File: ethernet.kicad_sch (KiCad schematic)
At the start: 94 parts, among them IC2 ACPL-217-500E, J2 5-2337992-8, U13 TPS2372-3RGWR, U16 TS3L500, U6 KSZ9031RNXCA, Y1 ABM8G-25.000MHZ-18-D2Y-T

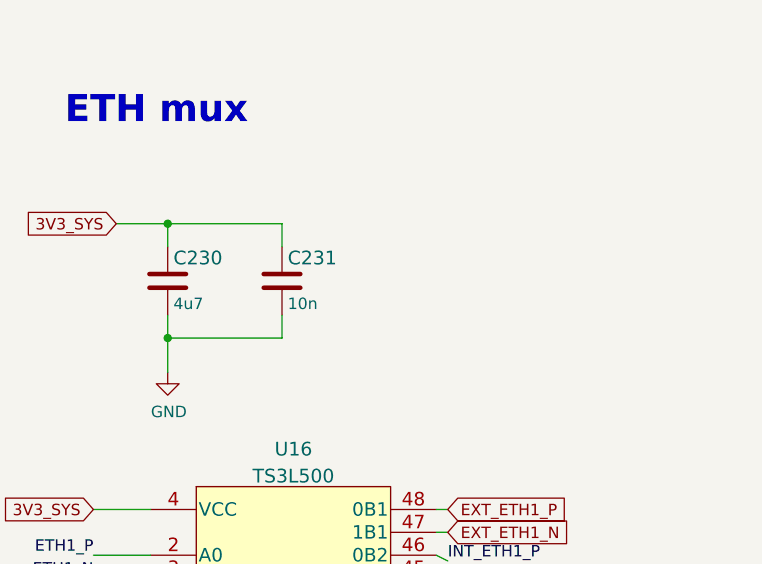
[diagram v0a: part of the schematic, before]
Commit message: Route internal end external (FMC) ETH interface, add additional VDDQ and ETH MUX decoupling
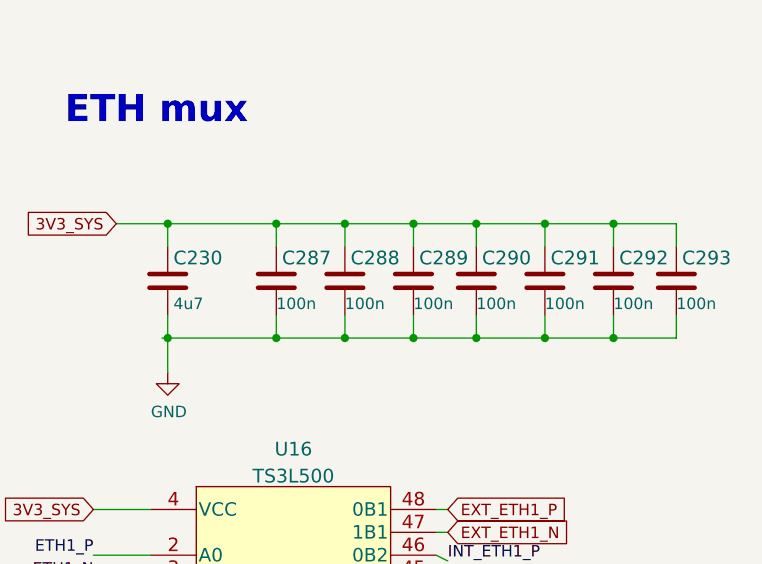
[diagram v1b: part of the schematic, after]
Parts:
- removed C231: C_10n_0402, data-center-dram-tester-footprints:0402-cap, symbol data-center-dram-tester:C_10n_0402
- added C287, C288, C289, C290, C291, C292, C293: C_100n_0402, antmicro-footprints:0402-cap, symbol antmicroCapacitors0402:C_100n_0402
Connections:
- net GND: now also C287.2, C288.2, C289.2, C290.2, C291.2, C292.2, C293.2
- net VCC: now also C287.1, C288.1, C289.1, C290.1, C291.1, C292.1, C293.1

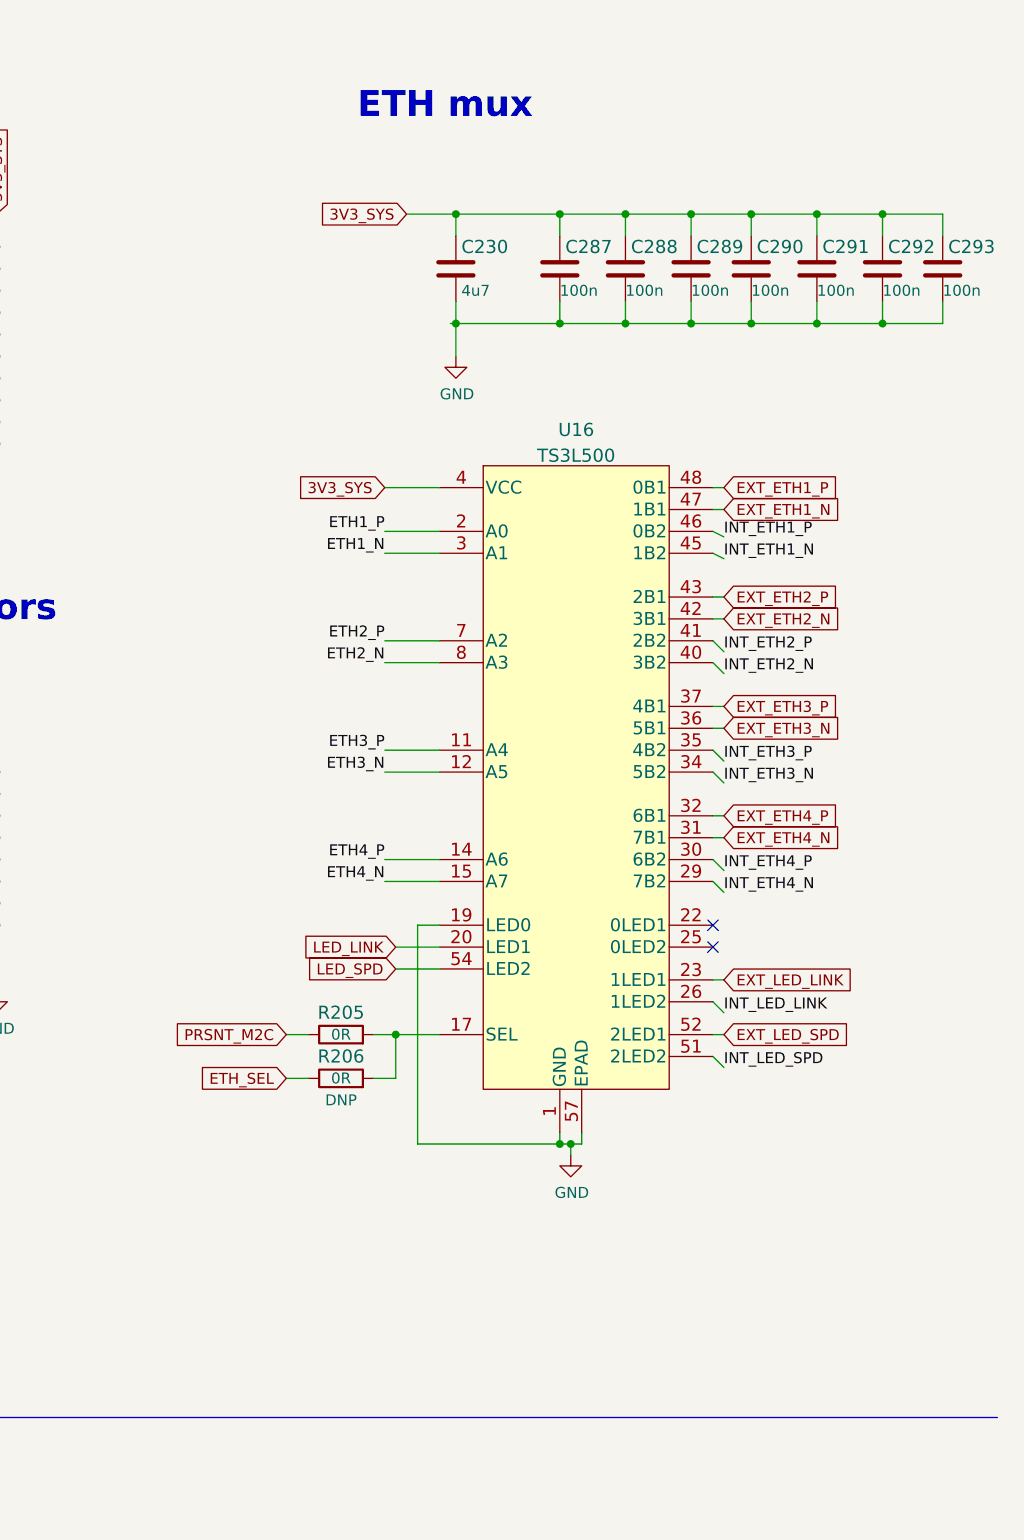
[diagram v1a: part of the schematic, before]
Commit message: Add ETH MUX passthrough, reroute HDMI to 100 Ohm differential, begin routing current measurment circuit
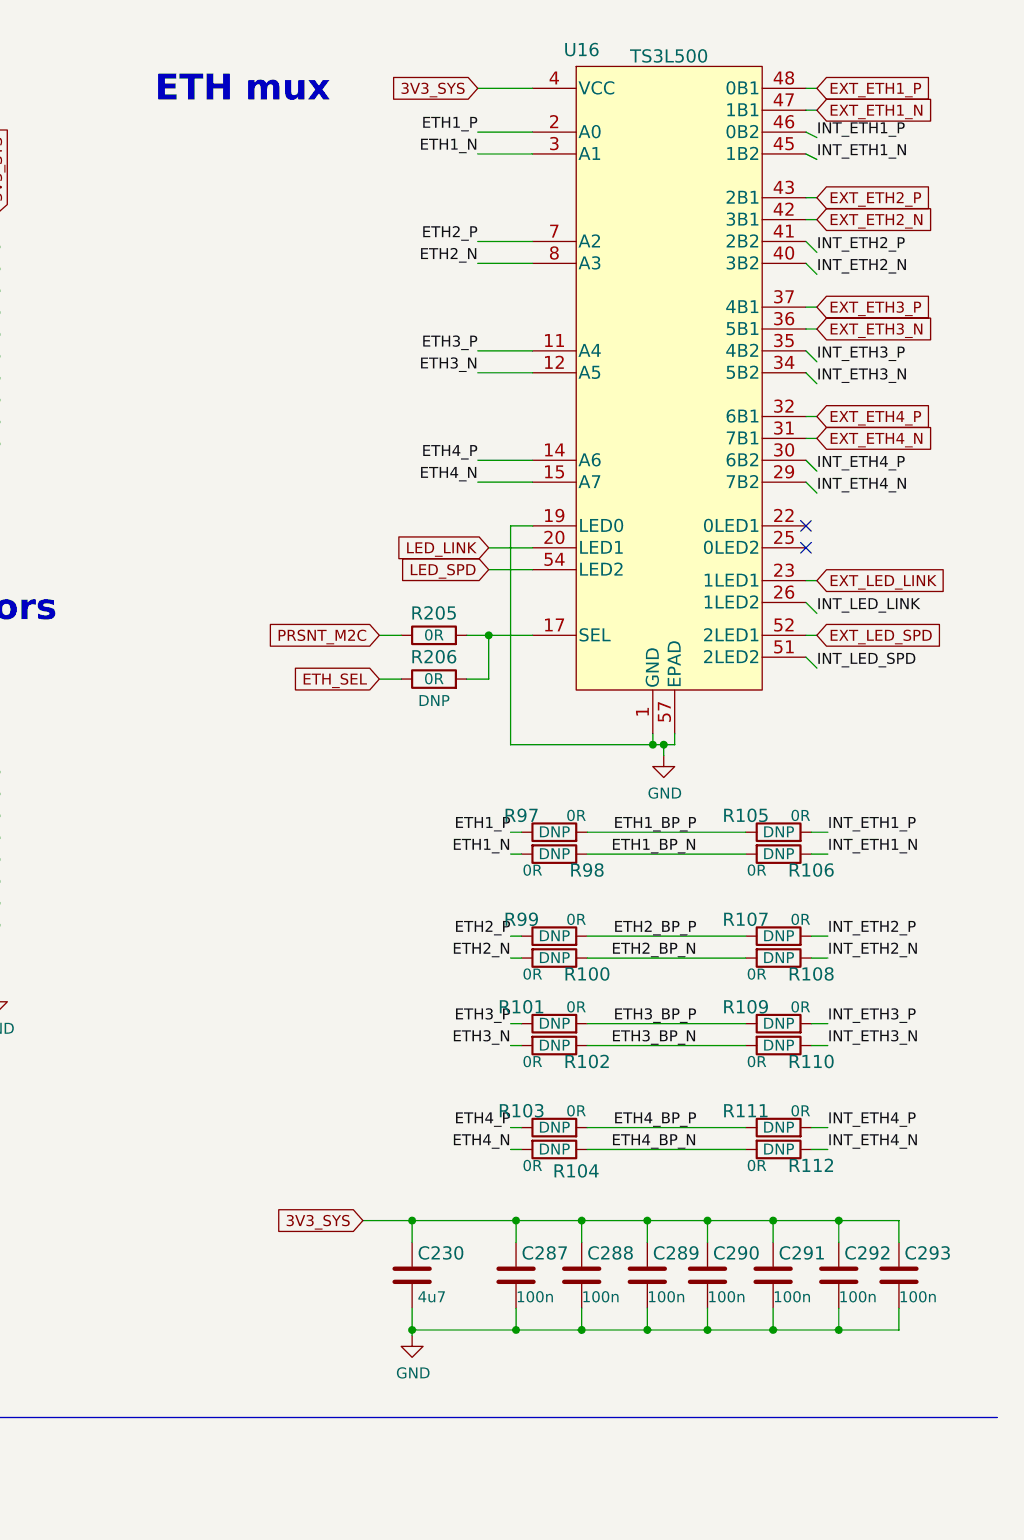
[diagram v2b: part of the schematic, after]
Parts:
- added R100, R101, R102, R103, R104, R105, R106, R107, R108, R109, R110, R111, R112, R97, R98, R99: R_0R_0201, antmicro-footprints:0201-res, symbol antmicroResistorsmisc:R_0R_0201
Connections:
- net ETH1_N: now also R98.2
- net ETH1_P: now also R97.1
- net ETH2_N: now also R100.2
- net ETH2_P: now also R99.1
- net ETH3_N: now also R102.2
- net ETH3_P: now also R101.1
- net ETH4_N: now also R104.2
- net ETH4_P: now also R103.1
- net INT_ETH1_N: now also R106.1
- net INT_ETH1_P: now also R105.2
- net INT_ETH2_N: now also R108.1
- net INT_ETH2_P: now also R107.2
- net INT_ETH3_N: now also R110.1
- net INT_ETH3_P: now also R109.2
- net INT_ETH4_N: now also R112.1
- net INT_ETH4_P: now also R111.2
- new net ETH1_BP_N: R106.2, R98.1
- new net ETH1_BP_P: R105.1, R97.2
- new net ETH2_BP_N: R100.1, R108.2
- new net ETH2_BP_P: R107.1, R99.2
- new net ETH3_BP_N: R102.1, R110.2
- new net ETH3_BP_P: R101.2, R109.1
- new net ETH4_BP_N: R104.1, R112.2
- new net ETH4_BP_P: R103.2, R111.1
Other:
- moved on the sheet: C230, C287, C288, C289, C290, C291, C292, C293, R205, R206, U16

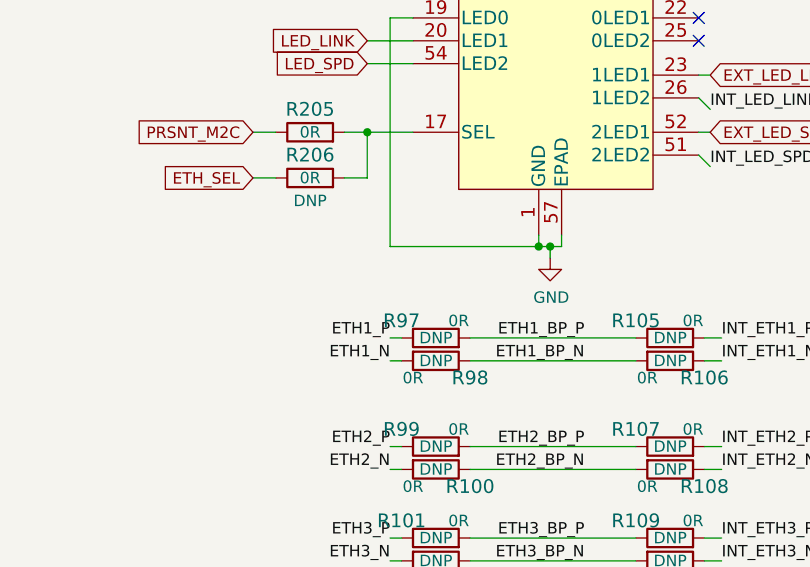
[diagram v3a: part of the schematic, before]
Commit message: Add missing FMC vias, route: MODE, JTAG, active discharge, reconnect 5V buses
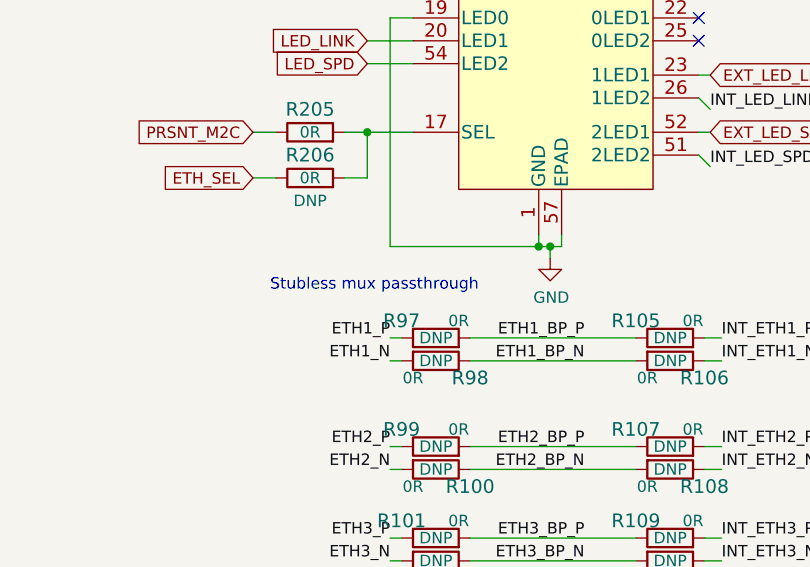
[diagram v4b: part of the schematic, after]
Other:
- note added: "Stubless mux passthrough"
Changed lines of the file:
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@@
     (effects (font (size 2.9972 2.9972) (thickness 0.5994) bold) (justify left bottom))
+  )
+  (text "Stubless mux passthrough" (at 339.09 102.235 0)
+    (effects (font (size 1.27 1.27)) (justify left bottom))
   )
   (label "INT_ETH4_N" (at 387.985 67.945 0)

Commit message: Finish power supply polygons, improve connector shield to ground connection
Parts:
- removed FB7: BLM18PG121SN1D, data-center-dram-tester-footprints:0603-res, symbol data-center-dram-tester:BLM18PG121SN1D
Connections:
- net GNDS: now reaches J2.19 (SHIELD1), J2.20 (SHIELD2)
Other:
- moved on the sheet: IC2, R183, R184

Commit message: Finish routing all connections
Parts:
- removed C221: C_10n_0402, data-center-dram-tester-footprints:0402-cap, symbol data-center-dram-tester:C_10n_0402
- added C221, C312: C_100n_0402, data-center-dram-tester-footprints:0402-cap, symbol data-center-dram-tester:C_100n_0402_16V
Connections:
- net GND: now also C221.2, C312.2
- net at J2.5 (P5): now also C312.1; no longer J2.4 (P4)
- new net: C221.1, J2.4 (P4)
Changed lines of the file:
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@@
   (junction (at 292.735 102.87) (diameter 0) (color 0 0 0 0)
   )
-  (junction (at 43.18 240.665) (diameter 0) (color 0 0 0 0)
-  )
   (junction (at 292.735 107.95) (diameter 0) (color 0 0 0 0)
   )
@@
   (junction (at 266.065 199.39) (diameter 0) (color 0 0 0 0)
   )
+  (junction (at 23.495 259.715) (diameter 0) (color 0 0 0 0)
+  )
   (junction (at 41.275 31.75) (diameter 0) (color 0 0 0 0)
   )
@@
     (stroke (width 0) (type default) (color 0 0 0 0))
   )
-  (wire (pts (xy 36.195 259.715) (xy 36.195 261.62))
+  (wire (pts (xy 23.495 255.905) (xy 23.495 259.715))
     (stroke (width 0) (type default) (color 0 0 0 0))
   )
@@
     (stroke (width 0) (type default) (color 0 0 0 0))
   )
-  (wire (pts (xy 44.45 243.205) (xy 43.18 243.205))
-    (stroke (width 0) (type default) (color 0 0 0 0))
-  )
   (wire (pts (xy 205.105 141.605) (xy 205.105 147.955))
     (stroke (width 0) (type default) (color 0 0 0 0))
@@
     (stroke (width 0) (type default) (color 0 0 0 0))
   )
+  (wire (pts (xy 31.75 243.205) (xy 31.75 248.285))
+    (stroke (width 0) (type default) (color 0 0 0 0))
+  )
   (wire (pts (xy 353.06 162.56) (xy 353.06 165.1))
     (stroke (width 0) (type default) (color 0 0 0 0))
@@
     (stroke (width 0) (type default) (color 0 0 0 0))
   )
-  (wire (pts (xy 43.18 240.665) (xy 43.18 243.205))
-    (stroke (width 0) (type default) (color 0 0 0 0))
-  )
   (wire (pts (xy 210.185 60.325) (xy 210.185 54.61))
     (stroke (width 0) (type default) (color 0 0 0 0))
@@
     (stroke (width 0) (type default) (color 0 0 0 0))
   )
+  (wire (pts (xy 23.495 259.715) (xy 31.75 259.715))
+    (stroke (width 0) (type default) (color 0 0 0 0))
+  )
   (wire (pts (xy 352.425 132.08) (xy 353.695 132.08))
     (stroke (width 0) (type default) (color 0 0 0 0))
@@
     (stroke (width 0) (type default) (color 0 0 0 0))
   )
+  (wire (pts (xy 31.75 243.205) (xy 44.45 243.205))
+    (stroke (width 0) (type default) (color 0 0 0 0))
+  )
   (wire (pts (xy 161.925 95.885) (xy 160.655 95.885))
     (stroke (width 0) (type default) (color 0 0 0 0))
@@
     (stroke (width 0) (type default) (color 0 0 0 0))
   )
-  (wire (pts (xy 44.45 240.665) (xy 43.18 240.665))
-    (stroke (width 0) (type default) (color 0 0 0 0))
-  )
   (wire (pts (xy 372.11 243.84) (xy 373.38 243.84))
     (stroke (width 0) (type default) (color 0 0 0 0))
@@
     (stroke (width 0) (type default) (color 0 0 0 0))
   )
+  (wire (pts (xy 31.75 259.715) (xy 31.75 255.905))
+    (stroke (width 0) (type default) (color 0 0 0 0))
+  )
   (wire (pts (xy 370.205 98.425) (xy 370.205 97.155))
     (stroke (width 0) (type default) (color 0 0 0 0))
@@
     (stroke (width 0) (type default) (color 0 0 0 0))
   )
+  (wire (pts (xy 23.495 259.715) (xy 23.495 261.62))
+    (stroke (width 0) (type default) (color 0 0 0 0))
+  )
   (wire (pts (xy 283.845 64.77) (xy 292.735 64.77))
     (stroke (width 0) (type default) (color 0 0 0 0))
@@
     (stroke (width 0) (type default) (color 0 0 0 0))
   )
+  (wire (pts (xy 23.495 240.665) (xy 44.45 240.665))
+    (stroke (width 0) (type default) (color 0 0 0 0))
+  )
   (wire (pts (xy 219.075 234.95) (xy 212.725 234.95))
     (stroke (width 0) (type default) (color 0 0 0 0))
@@
     (stroke (width 0) (type default) (color 0 0 0 0))
   )
-  (wire (pts (xy 36.195 240.665) (xy 36.195 252.095))
+  (wire (pts (xy 23.495 240.665) (xy 23.495 248.285))
     (stroke (width 0) (type default) (color 0 0 0 0))
   )
@@
     (stroke (width 0) (type default) (color 0 0 0 0))
   )
-  (wire (pts (xy 43.18 240.665) (xy 36.195 240.665))
-    (stroke (width 0) (type default) (color 0 0 0 0))
-  )
   (wire (pts (xy 387.985 48.895) (xy 386.715 48.895))
     (stroke (width 0) (type default) (color 0 0 0 0))
@@
     (pin "1")
   )
-  (symbol (lib_id "data-center-dram-tester:GND") (at 36.195 261.62 0) (unit 1)
+  (symbol (lib_id "data-center-dram-tester:GND") (at 23.495 261.62 0) (unit 1)
     (in_bom yes) (on_board yes)
-    (property "Reference" "#PWR042" (id 0) (at 36.195 267.97 0)
+    (property "Reference" "#PWR042" (id 0) (at 23.495 267.97 0)
       (effects (font (size 1.27 1.27)) hide)
     )
-    (property "Value" "GND" (id 1) (at 36.322 266.0142 0))
-    (property "Footprint" "" (id 2) (at 36.195 261.62 0)
+    (property "Value" "GND" (id 1) (at 23.622 266.0142 0))
+    (property "Footprint" "" (id 2) (at 23.495 261.62 0)
       (effects (font (size 1.27 1.27)) hide)
     )
-    (property "Datasheet" "" (id 3) (at 36.195 261.62 0)
+    (property "Datasheet" "" (id 3) (at 23.495 261.62 0)
       (effects (font (size 1.27 1.27)) hide)
     )
@@
     (pin "C")
   )
-  (symbol (lib_id "data-center-dram-tester:C_10n_0402") (at 36.195 255.905 0) (unit 1)
-    (in_bom yes) (on_board yes) (fields_autoplaced)
-    (property "Reference" "C221" (id 0) (at 33.2741 255.0704 0)
-      (effects (font (size 1.524 1.524)) (justify right))
-    )
-    (property "Value" "C_10n_0402" (id 1) (at 36.195 259.715 0)
-      (effects (font (size 1.524 1.524)) hide)
-    )
-    (property "Footprint" "data-center-dram-tester-footprints:0402-cap" (id 2) (at 41.275 250.825 0)
-      (effects (font (size 1.524 1.524)) (justify left) hide)
-    )
-    (property "Datasheet" "" (id 3) (at 36.195 255.905 0)
-      (effects (font (size 1.27 1.27)) hide)
-    )
-    (property "Manufacturer" "AVX" (id 4) (at 41.275 245.745 0)
-      (effects (font (size 1.524 1.524)) (justify left) hide)
-    )
-    (property "MPN" "04025G103ZAT2A" (id 5) (at 41.275 248.285 0)
-      (effects (font (size 1.524 1.524)) (justify left) hide)
-    )
-    (property "Val" "10n" (id 6) (at 33.2741 257.8355 0)
-      (effects (font (size 1.27 1.27)) (justify right))
-    )
-    (pin "1")
-    (pin "2")
-  )
   (symbol (lib_id "data-center-dram-tester:R_49k9_0402") (at 222.885 234.95 0) (unit 1)
     (in_bom yes) (on_board yes)
@@
     (pin "4")
   )
+  (symbol (lib_id "data-center-dram-tester:C_100n_0402_16V") (at 31.75 252.095 0) (unit 1)
+    (in_bom yes) (on_board yes)
+    (property "Reference" "C312" (id 0) (at 32.385 249.555 0)
+      (effects (font (size 1.524 1.524)) (justify left))
+    )
+    (property "Value" "C_100n_0402" (id 1) (at 31.75 255.905 0)
+      (effects (font (size 1.524 1.524)) hide)
+    )
+    (property "Footprint" "data-center-dram-tester-footprints:0402-cap" (id 2) (at 36.83 247.015 0)
+      (effects (font (size 1.524 1.524)) (justify left) hide)
+    )
+    (property "Datasheet" "" (id 3) (at 31.75 252.095 0)
+      (effects (font (size 1.27 1.27)) hide)
+    )
+    (property "Manufacturer" "MULTICOMP" (id 4) (at 36.83 241.935 0)
+      (effects (font (size 1.524 1.524)) (justify left) hide)
+    )
+    (property "MPN" "MC0402B104K160CT" (id 5) (at 36.83 244.475 0)
+      (effects (font (size 1.524 1.524)) (justify left) hide)
+    )
+    (property "Val" "100n" (id 6) (at 32.385 254.635 0)
+      (effects (font (size 1.27 1.27)) (justify left))
+    )
+    (pin "1")
+    (pin "2")
+  )
   (symbol (lib_id "antmicroResistorsmisc:R_0R_0201") (at 383.54 121.92 180) (unit 1)
     (in_bom yes) (on_board yes)
@@
     (pin "1")
   )
+  (symbol (lib_id "data-center-dram-tester:C_100n_0402_16V") (at 23.495 252.095 0) (unit 1)
+    (in_bom yes) (on_board yes)
+    (property "Reference" "C221" (id 0) (at 24.13 249.555 0)
+      (effects (font (size 1.524 1.524)) (justify left))
+    )
+    (property "Value" "C_100n_0402" (id 1) (at 23.495 255.905 0)
+      (effects (font (size 1.524 1.524)) hide)
+    )
+    (property "Footprint" "data-center-dram-tester-footprints:0402-cap" (id 2) (at 28.575 247.015 0)
+      (effects (font (size 1.524 1.524)) (justify left) hide)
+    )
+    (property "Datasheet" "" (id 3) (at 23.495 252.095 0)
+      (effects (font (size 1.27 1.27)) hide)
+    )
+    (property "Manufacturer" "MULTICOMP" (id 4) (at 28.575 241.935 0)
+      (effects (font (size 1.524 1.524)) (justify left) hide)
+    )
+    (property "MPN" "MC0402B104K160CT" (id 5) (at 28.575 244.475 0)
+      (effects (font (size 1.524 1.524)) (justify left) hide)
+    )
+    (property "Val" "100n" (id 6) (at 24.13 254.635 0)
+      (effects (font (size 1.27 1.27)) (justify left))
+    )
+    (pin "1")
+    (pin "2")
+  )
   (symbol (lib_id "data-center-dram-tester:PTVS58VS1UR,115") (at 198.12 210.185 90) (unit 1)

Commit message: Minor readability improvements
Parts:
- Y1: VAL (none) -> 25MHz
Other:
- moved on the sheet: C120, C121, C122, C124, C125, C126, C127, C128, C129, C130, C131, C133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
